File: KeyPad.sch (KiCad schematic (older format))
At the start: 9 parts, among them P1 CONN_01X03, SW1 SW_Push_Dual, SW2 SW_Push_Dual, SW3 SW_Push_Dual, SW4 SW_Push_Dual

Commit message: archivos estandarizados para compartir
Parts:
- P1: footprint Connectors_JST:JST_PH_S3B-PH-K_03x2.00mm_Angled -> lib_fp:JST_PH_S3B-PH-K_03x2.00mm_Angled
- R1, R2, R3, R4: footprint Resistors_SMD:R_0805 -> lib_fp:R_0805
- SW1, SW2, SW3, SW4: footprint Buttons_Switches_THT:SW_PUSH-12mm -> lib_fp:SW_PUSH-12mm
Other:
- moved on the sheet: R1, R2, R3, R4

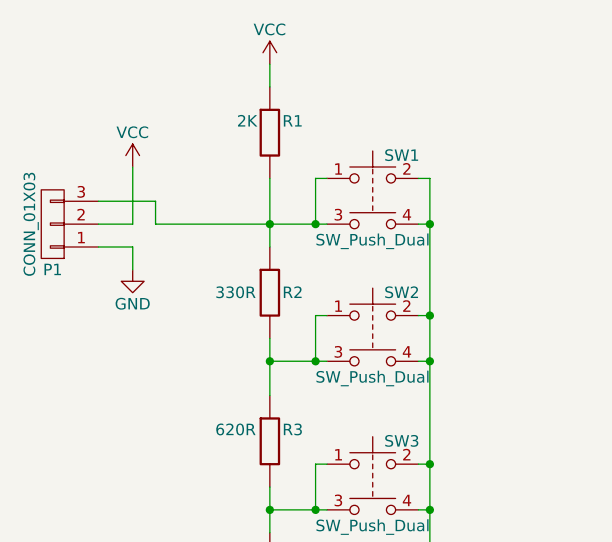
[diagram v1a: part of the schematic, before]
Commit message: conector cambiado
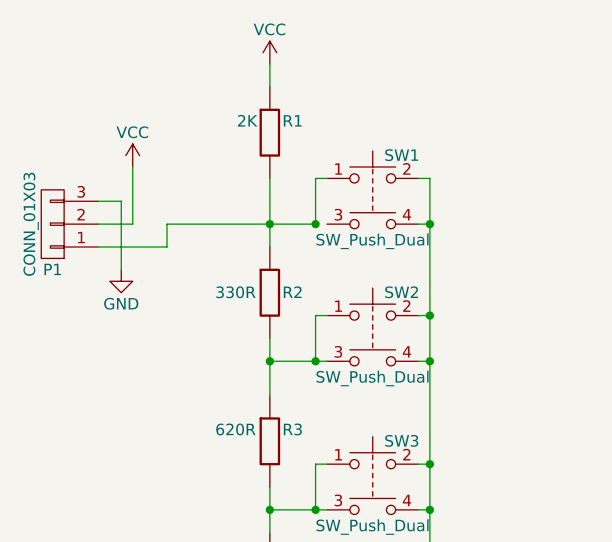
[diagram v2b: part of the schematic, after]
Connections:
- net GND: now also P1.3 (P3); no longer P1.1 (P1)
- net at R1.2, R2.1, SW1.1: now also P1.1 (P1); no longer P1.3 (P3), SW1.3
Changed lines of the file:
@@
 EESchema Schematic File Version 2
+LIBS:KeyPad
 LIBS:5050_ws2811
 LIBS:a4988-module
@@
 LIBS:Sensor_Current
 LIBS:Sensor_Humidity
-LIBS:smd oscillator
 LIBS:songle_relay
 LIBS:SparkFun-Aesthetics
@@
 LIBS:zetex
 LIBS:Zilog
-LIBS:KeyPad-cache
 EELAYER 25 0
 EELAYER END
@@
 L GND-RESCUE-KeyPad #PWR03
 U 1 1 58F1101F
-P 4600 3100
-F 0 "#PWR03" H 4600 2850 50  0001 C CNN
-F 1 "GND" H 4600 2950 50  0000 C CNN
-F 2 "" H 4600 3100 50  0001 C CNN
-F 3 "" H 4600 3100 50  0001 C CNN
-	1    4600 3100
-	1    0    0    -1
-$EndComp
-Wire Wire Line
-	4450 3000 4600 3000
-Wire Wire Line
-	4600 3000 4600 3100
+P 4550 3100
+F 0 "#PWR03" H 4550 2850 50  0001 C CNN
+F 1 "GND" H 4550 2950 50  0000 C CNN
+F 2 "" H 4550 3100 50  0001 C CNN
+F 3 "" H 4550 3100 50  0001 C CNN
+	1    4550 3100
+	1    0    0    -1
+$EndComp
 $Comp
 L VCC #PWR04
@@
 	6400 6850 6400 7150
 Wire Wire Line
-	4700 2900 5450 2900
-Wire Wire Line
-	4700 2900 4700 2800
-Wire Wire Line
-	4700 2800 4450 2800
-Wire Wire Line
 	4600 2650 4600 2900
 Wire Wire Line
@@
 Wire Wire Line
 	5200 2300 5200 2200
+Wire Wire Line
+	5400 2900 4750 2900
+Wire Wire Line
+	4750 2900 4750 3000
+Wire Wire Line
+	4750 3000 4450 3000
+Wire Wire Line
+	4550 3100 4550 2800
+Wire Wire Line
+	4550 2800 4450 2800
 $EndSCHEMATC
